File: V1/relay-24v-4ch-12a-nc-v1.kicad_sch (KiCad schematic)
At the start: 23 parts, among them J1 DG141V-2.54-6P, J2 DB142V-5.08-4P, J3 DB142V-5.08-4P, K1 Songle_SRD_1B, K2 Songle_SRD_1B, K3 Songle_SRD_1B, K4 Songle_SRD_1B

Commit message: Creating layout
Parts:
- removed J1: DG141V-2.54-6P, Tales:TerminalBlock_Dibo_DB141V-2.54-6P_1x06_P2.54mm_Vertical, symbol Connector_Generic:Conn_01x06
- added J1: DB141V-2.54-2P, Tales:TerminalBlock_Dibo_DB141V-2.54-2P_1x02_P2.54mm_Vertical, symbol Connector_Generic:Conn_01x02
- added J2: DB141V-2.54-4P, Tales:TerminalBlock_Dibo_DB141V-2.54-4P_1x04_P2.54mm_Vertical, symbol Connector_Generic:Conn_01x04
- renumbered J2 to J3, J3 to J4
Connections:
- net +24V: now also J1.1 (Pin_1), J1.2 (Pin_2)
- net at D7.1 (K), D8.2 (A), K4.A2: now also J2.4 (Pin_4)
- net at D1.1 (K), D2.2 (A), K1.A2: now also J2.1 (Pin_1)
- net at D5.1 (K), D6.2 (A), K3.A2: now also J2.3 (Pin_3)
- net at D3.1 (K), D4.2 (A), K2.A2: now also J2.2 (Pin_2)

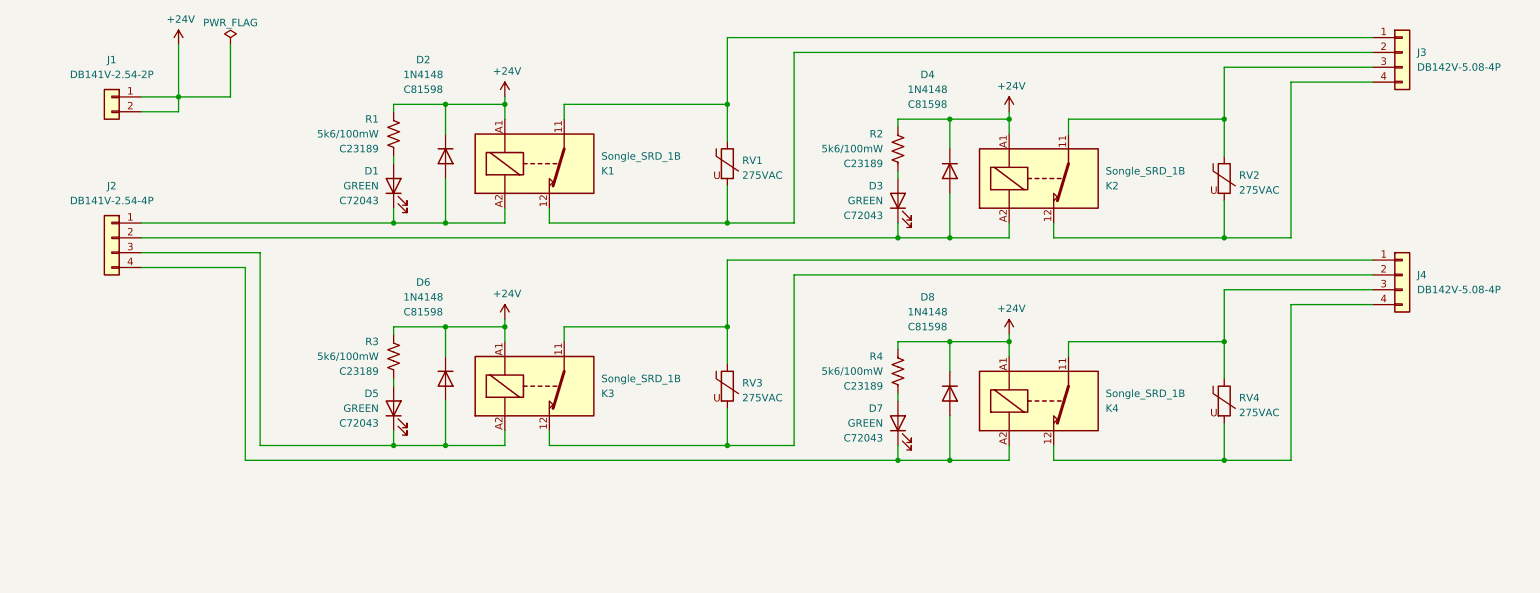
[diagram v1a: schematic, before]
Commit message: Updated connectors
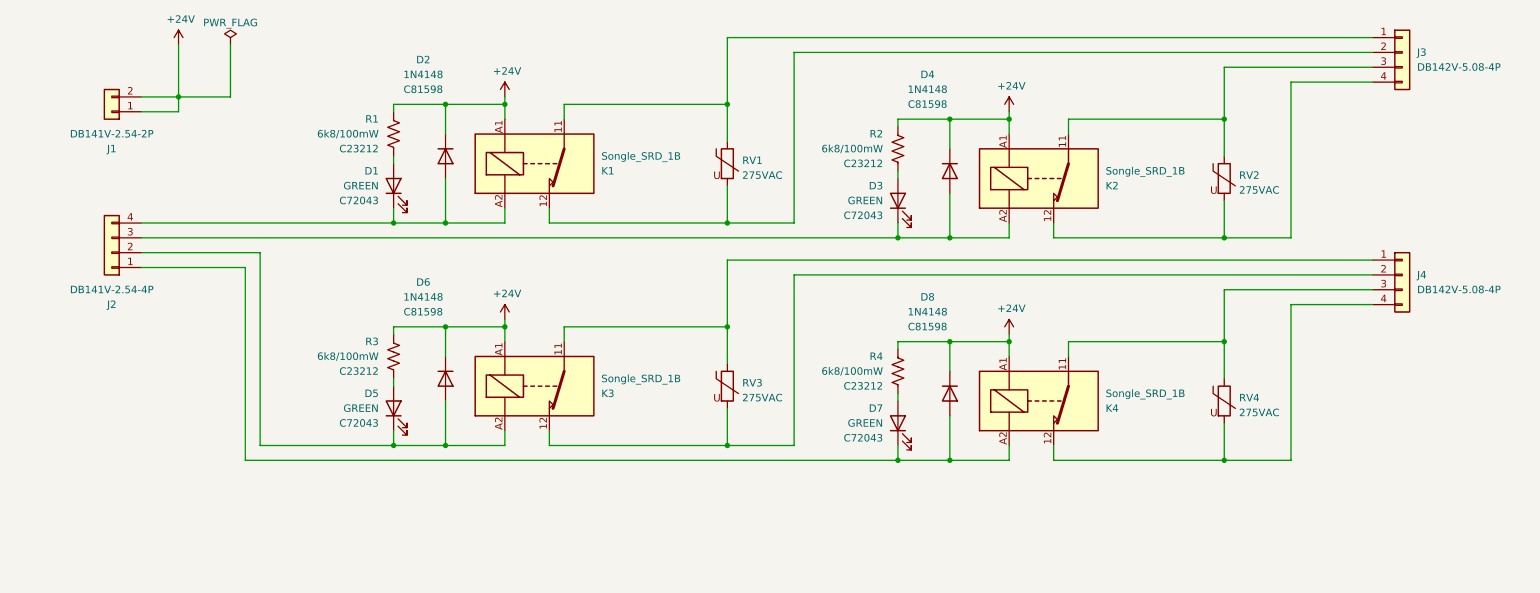
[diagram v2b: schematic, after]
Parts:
- R1, R2, R3, R4: value 5k6/100mW -> 6k8/100mW; LCSC Part # C23189 -> C23212; Mfr PN 0805W8F4701T5E -> 0603WAF6801T5E; Vendor PN C23189 -> C23212
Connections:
- net at D7.1 (K), D8.2 (A), K4.A2: now also J2.1 (Pin_1); no longer J2.4 (Pin_4)
- net at D1.1 (K), D2.2 (A), K1.A2: now also J2.4 (Pin_4); no longer J2.1 (Pin_1)
- net at D5.1 (K), D6.2 (A), K3.A2: now also J2.2 (Pin_2); no longer J2.3 (Pin_3)
- net at D3.1 (K), D4.2 (A), K2.A2: now also J2.3 (Pin_3); no longer J2.2 (Pin_2)
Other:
- moved on the sheet: J1, J2
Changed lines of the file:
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@@
 	(symbol
 		(lib_id "Connector_Generic:Conn_01x04")
-		(at 35.56 88.9 0)
-		(mirror y)
+		(at 35.56 91.44 180)
 		(unit 1)
 		(exclude_from_sim no)
@@
 		(on_board yes)
 		(dnp no)
-		(fields_autoplaced yes)
 		(property "Reference" "J2"
-			(at 35.56 80.01 0)
+			(at 35.56 100.33 0)
 			(effects
 				(font
@@
 		)
 		(property "Value" "DB141V-2.54-4P"
-			(at 35.56 82.55 0)
+			(at 35.56 97.79 0)
 			(effects
 				(font
@@
 		)
 		(property "Footprint" "Tales:TerminalBlock_Dibo_DB141V-2.54-4P_1x04_P2.54mm_Vertical"
-			(at 35.56 88.9 0)
+			(at 35.56 91.44 0)
 			(effects
 				(font
@@
 		)
 		(property "Datasheet" "~"
-			(at 35.56 88.9 0)
+			(at 35.56 91.44 0)
 			(effects
 				(font
@@
 		)
 		(property "Description" ""
-			(at 35.56 88.9 0)
+			(at 35.56 91.44 0)
 			(effects
 				(font
@@
 			)
 		)
-		(property "Value" "5k6/100mW"
+		(property "Value" "6k8/100mW"
 			(at 81.28 71.12 0)
 			(effects
@@
 			)
 		)
-		(property "Mfr PN" "0805W8F4701T5E"
+		(property "Mfr PN" "0603WAF6801T5E"
 			(at 83.82 71.12 0)
 			(effects
@@
 			)
 		)
-		(property "Vendor PN" "C23189"
+		(property "Vendor PN" "C23212 "
 			(at 83.82 71.12 0)
 			(effects
@@
 			)
 		)
-		(property "LCSC Part #" "C23189"
+		(property "LCSC Part #" "C23212"
 			(at 81.28 73.66 0)
 			(effects
@@
 			)
 		)
-		(property "Value" "5k6/100mW"
+		(property "Value" "6k8/100mW"
 			(at 81.28 109.22 0)
 			(effects
@@
 			)
 		)
-		(property "Mfr PN" "0805W8F4701T5E"
+		(property "Mfr PN" "0603WAF6801T5E"
 			(at 83.82 109.22 0)
 			(effects
@@
 			)
 		)
-		(property "Vendor PN" "C23189"
+		(property "Vendor PN" "C23212 "
 			(at 83.82 109.22 0)
 			(effects
@@
 			)
 		)
-		(property "LCSC Part #" "C23189"
+		(property "LCSC Part #" "C23212"
 			(at 81.28 111.76 0)
 			(effects
@@
 	(symbol
 		(lib_id "Connector_Generic:Conn_01x02")
-		(at 35.56 64.77 0)
-		(mirror y)
+		(at 35.56 67.31 180)
 		(unit 1)
 		(exclude_from_sim no)
@@
 		(on_board yes)
 		(dnp no)
-		(fields_autoplaced yes)
 		(property "Reference" "J1"
-			(at 35.56 58.42 0)
+			(at 35.56 73.66 0)
 			(effects
 				(font
@@
 		)
 		(property "Value" "DB141V-2.54-2P"
-			(at 35.56 60.96 0)
+			(at 35.56 71.12 0)
 			(effects
 				(font
@@
 		)
 		(property "Footprint" "Tales:TerminalBlock_Dibo_DB141V-2.54-2P_1x02_P2.54mm_Vertical"
-			(at 35.56 64.77 0)
+			(at 35.56 67.31 0)
 			(effects
 				(font
@@
 		)
 		(property "Datasheet" "~"
-			(at 35.56 64.77 0)
+			(at 35.56 67.31 0)
 			(effects
 				(font
@@
 		)
 		(property "Description" ""
-			(at 35.56 64.77 0)
+			(at 35.56 67.31 0)
 			(effects
 				(font
@@
 			)
 		)
-		(property "Value" "5k6/100mW"
+		(property "Value" "6k8/100mW"
 			(at 167.64 111.76 0)
 			(effects
@@
 			)
 		)
-		(property "Mfr PN" "0805W8F4701T5E"
+		(property "Mfr PN" "0603WAF6801T5E"
 			(at 170.18 111.76 0)
 			(effects
@@
 			)
 		)
-		(property "Vendor PN" "C23189"
+		(property "Vendor PN" "C23212 "
 			(at 170.18 111.76 0)
 			(effects
@@
 			)
 		)
-		(property "LCSC Part #" "C23189"
+		(property "LCSC Part #" "C23212"
 			(at 167.64 114.3 0)
 			(effects
@@
 			)
 		)
-		(property "Value" "5k6/100mW"
+		(property "Value" "6k8/100mW"
 			(at 167.64 73.66 0)
 			(effects
@@
 			)
 		)
-		(property "Mfr PN" "0805W8F4701T5E"
+		(property "Mfr PN" "0603WAF6801T5E"
 			(at 170.18 73.66 0)
 			(effects
@@
 			)
 		)
-		(property "Vendor PN" "C23189"
+		(property "Vendor PN" "C23212 "
 			(at 170.18 73.66 0)
 			(effects
@@
 			)
 		)
-		(property "LCSC Part #" "C23189"
+		(property "LCSC Part #" "C23212"
 			(at 167.64 76.2 0)
 			(effects

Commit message: Review before fabrication
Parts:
- J1, J2: JLCPCB BOM (none) -> 1; Mfr (none) -> DORABO; Vendor (none) -> JLCPCB
- R1, R2, R3, R4: value 6k8/100mW -> 10k/100mW; LCSC Part # C23212 -> C25804; Mfr Uniroyal -> UNI-ROYAL(Uniroyal Elec); Mfr PN 0603WAF6801T5E -> 0603WAF1002T5E; Vendor PN C23212 -> C25804
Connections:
- net IN4: now reaches D7.1 (K), D8.2 (A), J2.1 (Pin_1), K4.A2
- net LED4: now reaches D7.2 (A), R4.2
- net IN1: now reaches D1.1 (K), D2.2 (A), J2.4 (Pin_4), K1.A2
- net OUT3PW: now reaches J4.1 (Pin_1), K3.11, RV3.1
- net OUT3LD: now reaches J4.2 (Pin_2), K3.12, RV3.2
- net IN3: now reaches D5.1 (K), D6.2 (A), J2.2 (Pin_2), K3.A2
- net IN2: now reaches D3.1 (K), D4.2 (A), J2.3 (Pin_3), K2.A2
- net OUT2PW: now reaches J3.3 (Pin_3), K2.11, RV2.1
- net OUT2LD: now reaches J3.4 (Pin_4), K2.12, RV2.2
- net LED1: now reaches D1.2 (A), R1.2
- net LED3: now reaches D5.2 (A), R3.2
- net OUT1PW: now reaches J3.1 (Pin_1), K1.11, RV1.1
- net OUT1LD: now reaches J3.2 (Pin_2), K1.12, RV1.2
- net OUT4PW: now reaches J4.3 (Pin_3), K4.11, RV4.1
- net OUT4LD: now reaches J4.4 (Pin_4), K4.12, RV4.2
- net LED2: now reaches D3.2 (A), R2.2
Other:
- moved on the sheet: D1, D2, D3, D4, D5, D6, D7, D8, J1, J2, J3, J4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

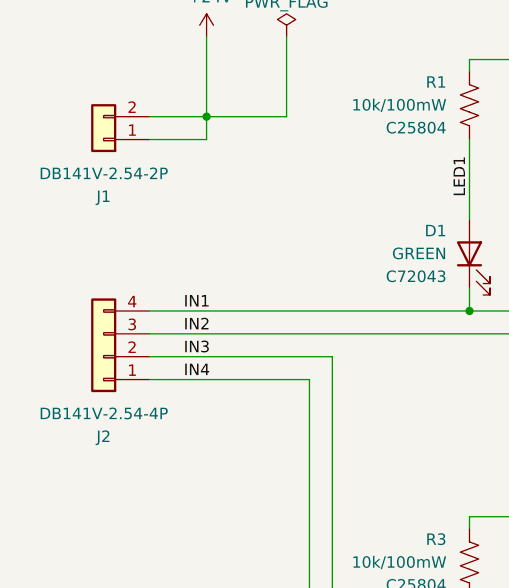
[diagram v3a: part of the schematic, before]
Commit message: Replaced input terminal blocks for 3.5mm pitch.
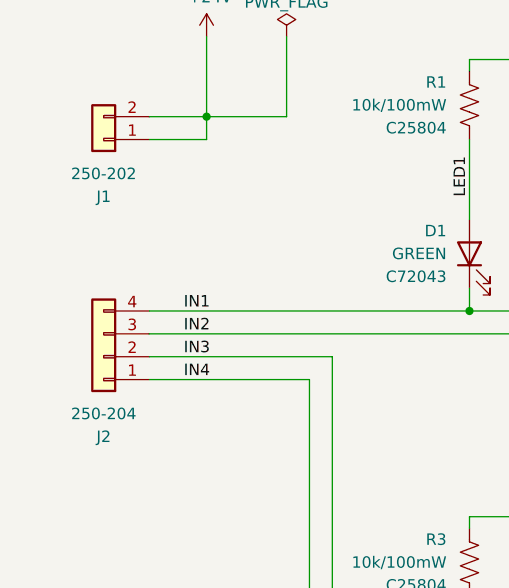
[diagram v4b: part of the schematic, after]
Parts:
- J1: value DB141V-2.54-2P -> 250-202; footprint Tales:TerminalBlock_Dibo_DB141V-2.54-2P_1x02_P2.54mm_Vertical -> Tales:TerminalBlock_Wago_250-202_1x02_P3.5mm_45Degree; LCSC Part # (none) -> C2765061; Mfr DORABO -> Wago; Mfr PN (none) -> 250-202; Vendor PN (none) -> C2765061
- J2: value DB141V-2.54-4P -> 250-204; footprint Tales:TerminalBlock_Dibo_DB141V-2.54-4P_1x04_P2.54mm_Vertical -> Tales:TerminalBlock_Wago_250-204_1x04_P3.5mm_45Degree; LCSC Part # (none) -> C2765063; Mfr DORABO -> Wago; Mfr PN (none) -> 250-204; Vendor PN (none) -> C2765063
